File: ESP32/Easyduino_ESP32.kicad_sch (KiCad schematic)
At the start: 27 parts, among them J1 USB_C_Receptacle_USB2.0, Q1 SS8050, Q2 SS8050, SW1 SW_Push, SW2 SW_Push, U1 CP2102N-Axx-xQFN28, U2 ESP32-WROOM-E, U3 AMS1117-3.3, U4 ESP32-DevKitC

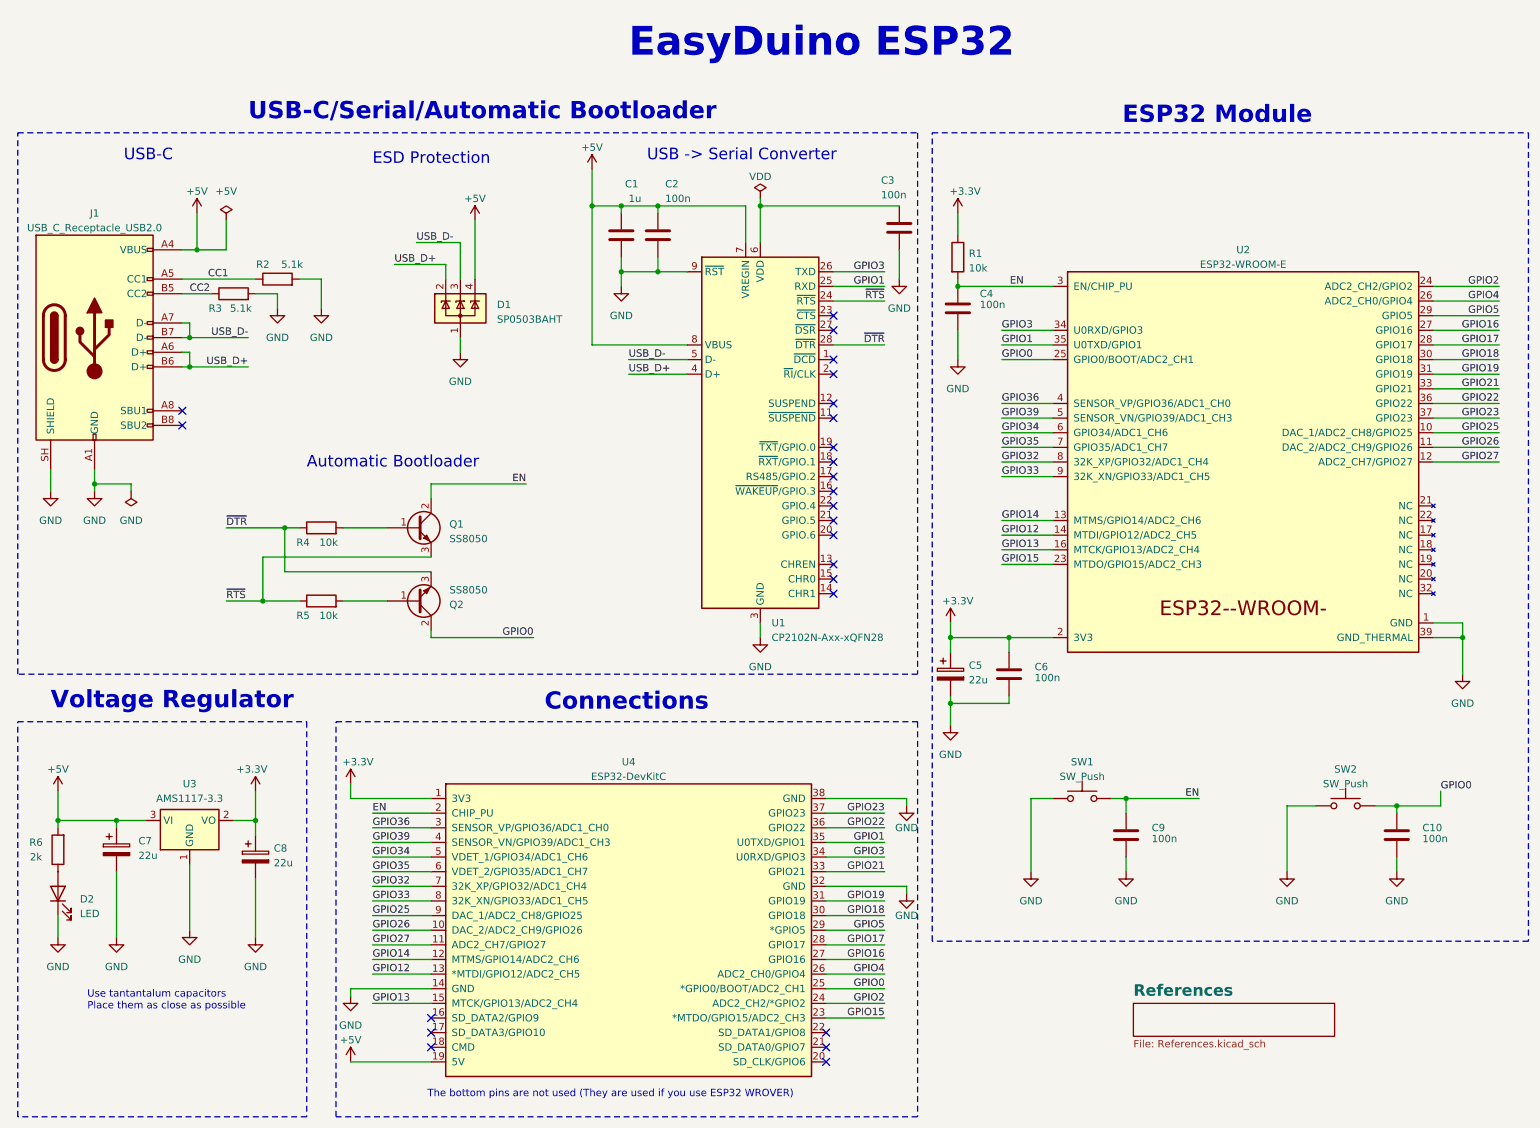
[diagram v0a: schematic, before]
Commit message: ESP32 CP2102 bugfix
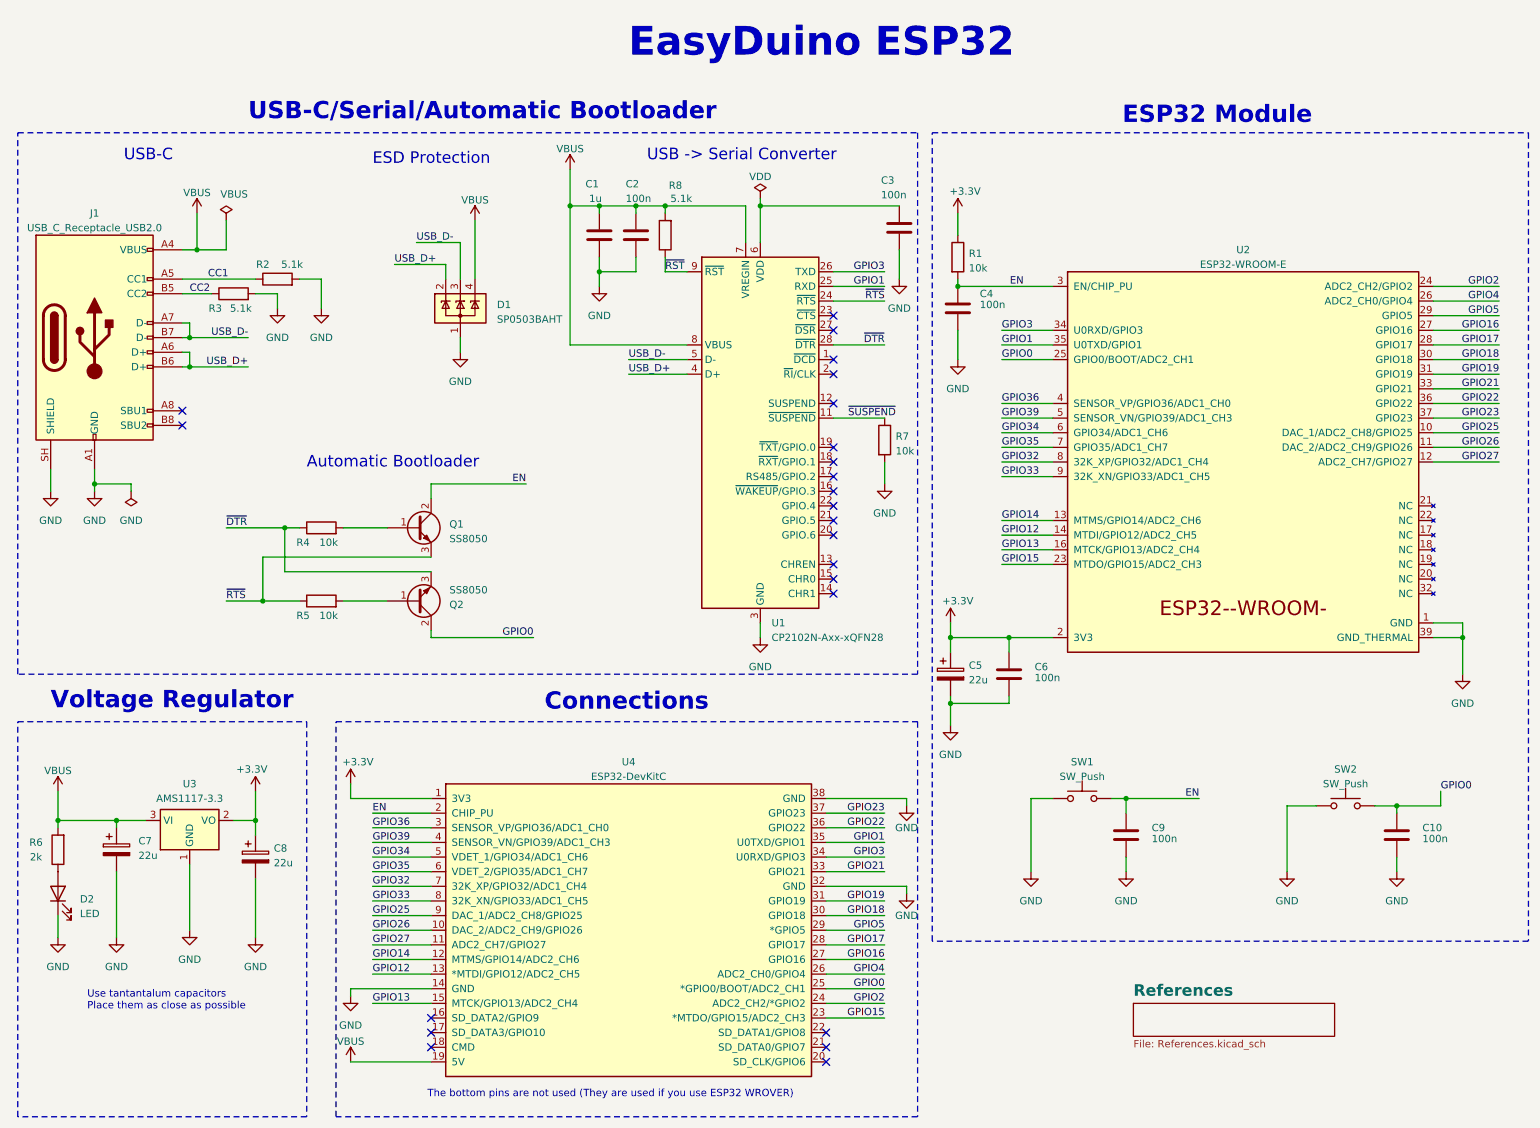
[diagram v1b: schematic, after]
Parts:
- added R7: 10k, Resistor_SMD:R_0402_1005Metric, symbol Device:R
- added R8: 5.1k, Resistor_SMD:R_0402_1005Metric, symbol Device:R
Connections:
- net GND: now also R7.2; no longer U1.9 (~{RST})
- net ~{SUSPEND}: now reaches U1.11 (~{SUSPEND})
- net ~{SUSPEND}: now also R7.1
- net +5V renamed VBUS
- net VBUS: now also R8.2
- new net ~{RST}: R8.1, U1.9 (~{RST})
- no-connect marks 24 -> 23
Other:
- moved on the sheet: C1, C2
